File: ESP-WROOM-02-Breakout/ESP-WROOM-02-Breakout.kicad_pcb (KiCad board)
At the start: 2 copper layers, 31.5 x 29 mm, 9 parts, among them IC1 ESP-WROOM-02U__4MB_, J1 Left Pins, J2 Right Pins, J3 UART

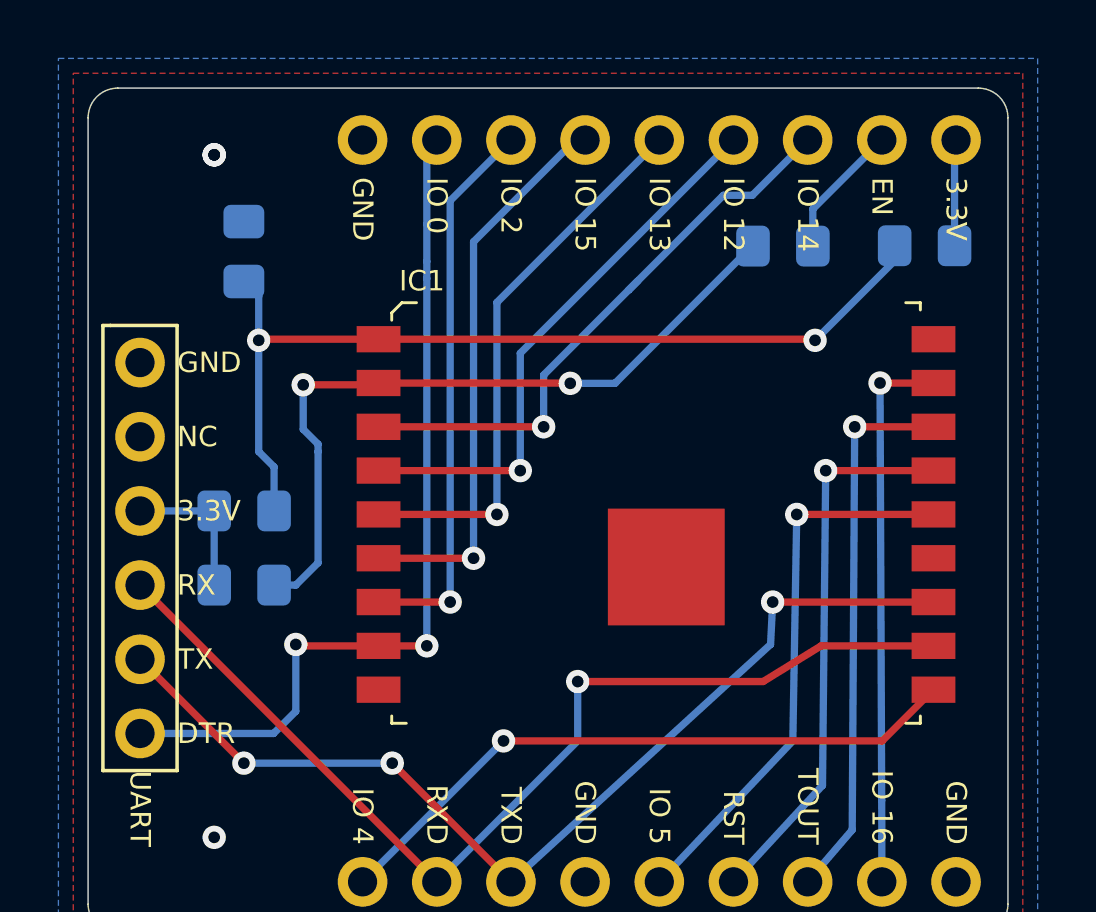
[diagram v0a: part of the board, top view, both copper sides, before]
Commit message: improve esp footprint, small fixes
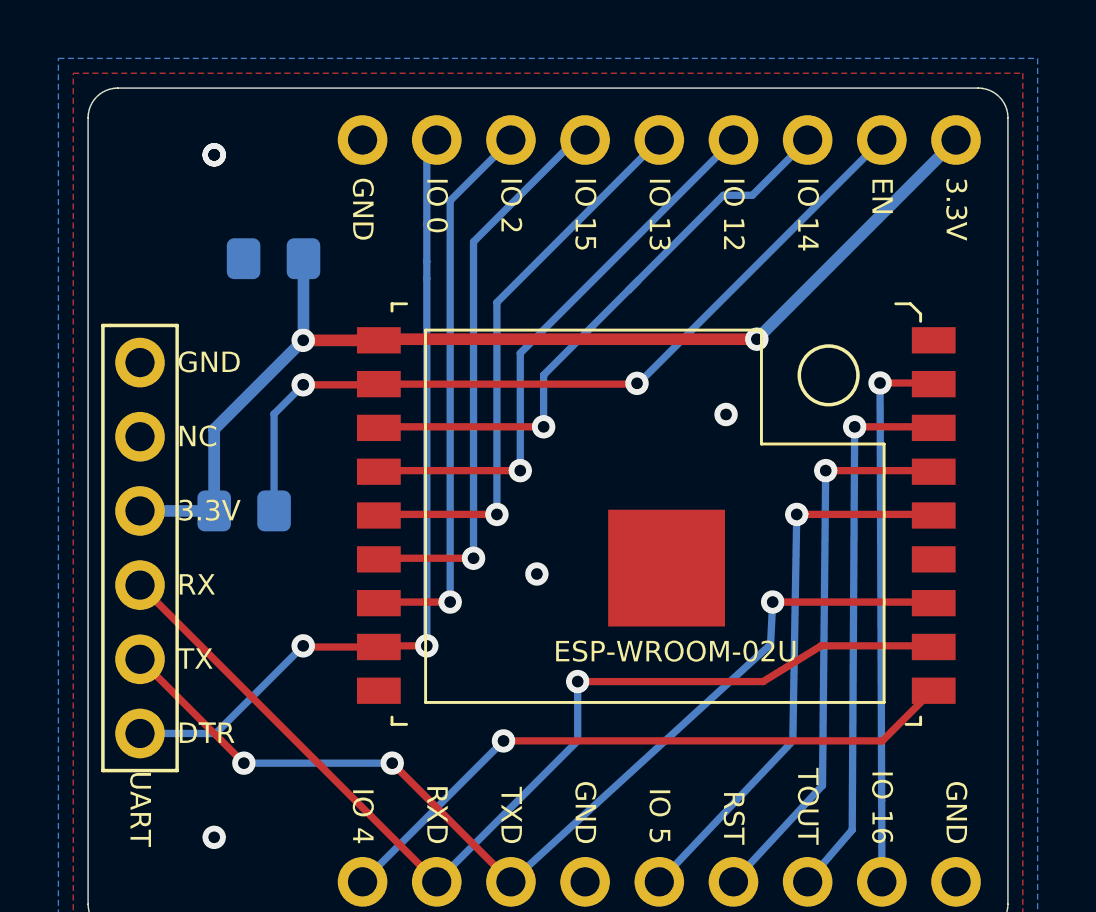
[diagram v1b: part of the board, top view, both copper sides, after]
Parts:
- removed D1, D2, D3: D, Diode_SMD:D_0805_2012Metric_Pad1.15x1.40mm_HandSolder
- moved IC1 8.28 mm to (60.3, 30.6)
- moved R1 2.54 mm to (46.7, 30.5), turned to 0 degrees
- moved C1 1.05 mm to (47.8, 21.8), turned to 180 degrees
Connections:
- C1 pad 1: Net-(C1-Pad1) -> +3V3
- IC1 pad 1: Net-(C1-Pad1) -> +3V3
- IC1 pad 2: Net-(D3-Pad1) -> Net-(IC1-Pad2)
- J1 pad 8: Net-(D3-Pad2) -> Net-(IC1-Pad2)
- J1 pad 9: Net-(D2-Pad2) -> +3V3
- J3 pad 4: Net-(D1-Pad2) -> +3V3
- R1 pad 1: Net-(D3-Pad1) -> +3V3
- R1 pad 2: Net-(D1-Pad2) -> Net-(IC1-Pad2)
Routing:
- net +3V3: track 0.00 -> 37.7 mm, vias 0 -> 2
- net Net-(C1-Pad1): track 31.7 -> 0.00 mm, vias 2 -> 0
- net Net-(IC1-Pad2): track 0.00 -> 28.0 mm, vias 0 -> 2
- net Net-(D3-Pad1): track 25.5 -> 0.00 mm, vias 2 -> 0
- net Net-(D1-Pad2): track 5.08 -> 0.00 mm
- net Net-(D3-Pad2): track 4.64 -> 0.00 mm
- net Net-(D2-Pad2): track 3.67 -> 0.00 mm
- net Net-(IC1-Pad8): track 30.8 -> 29.4 mm
- net GNDREF: vias 3 -> 5

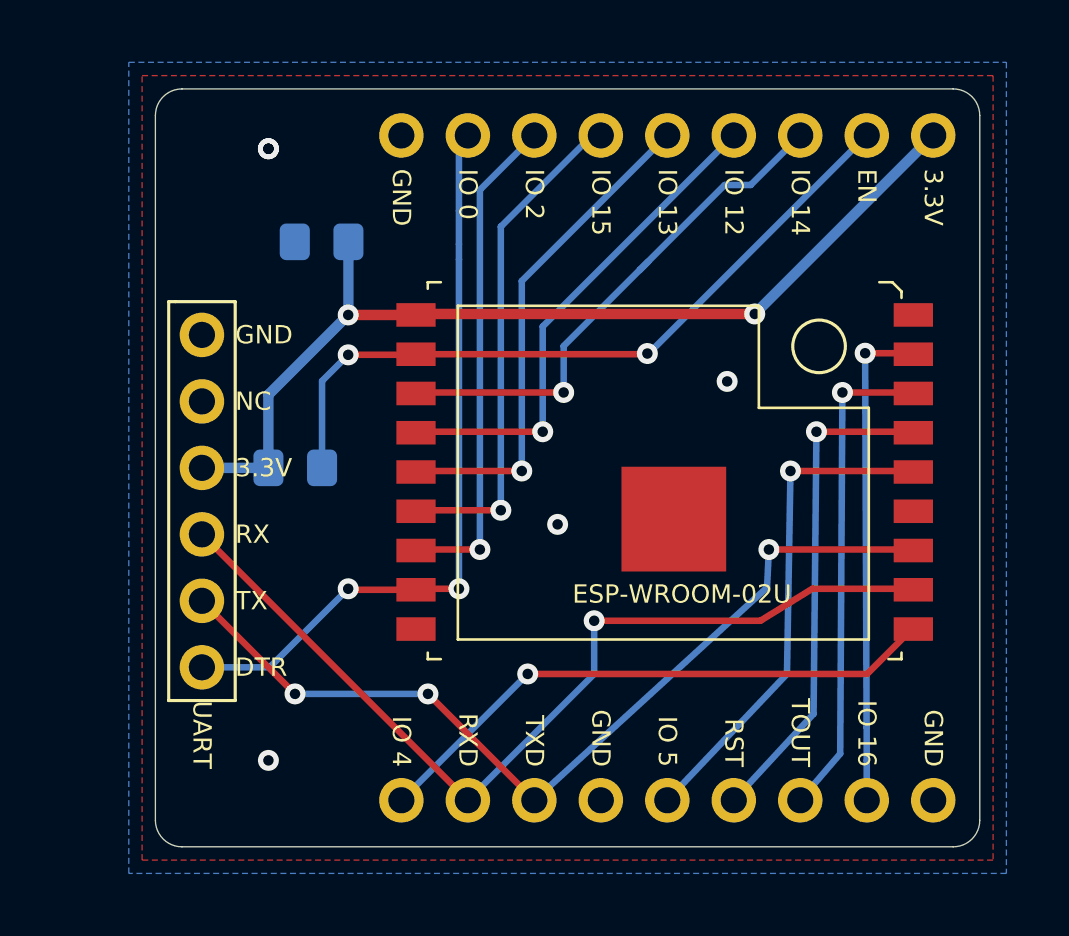
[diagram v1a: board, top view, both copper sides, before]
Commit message: move all components to one side, try to keep it hand-solder friendly
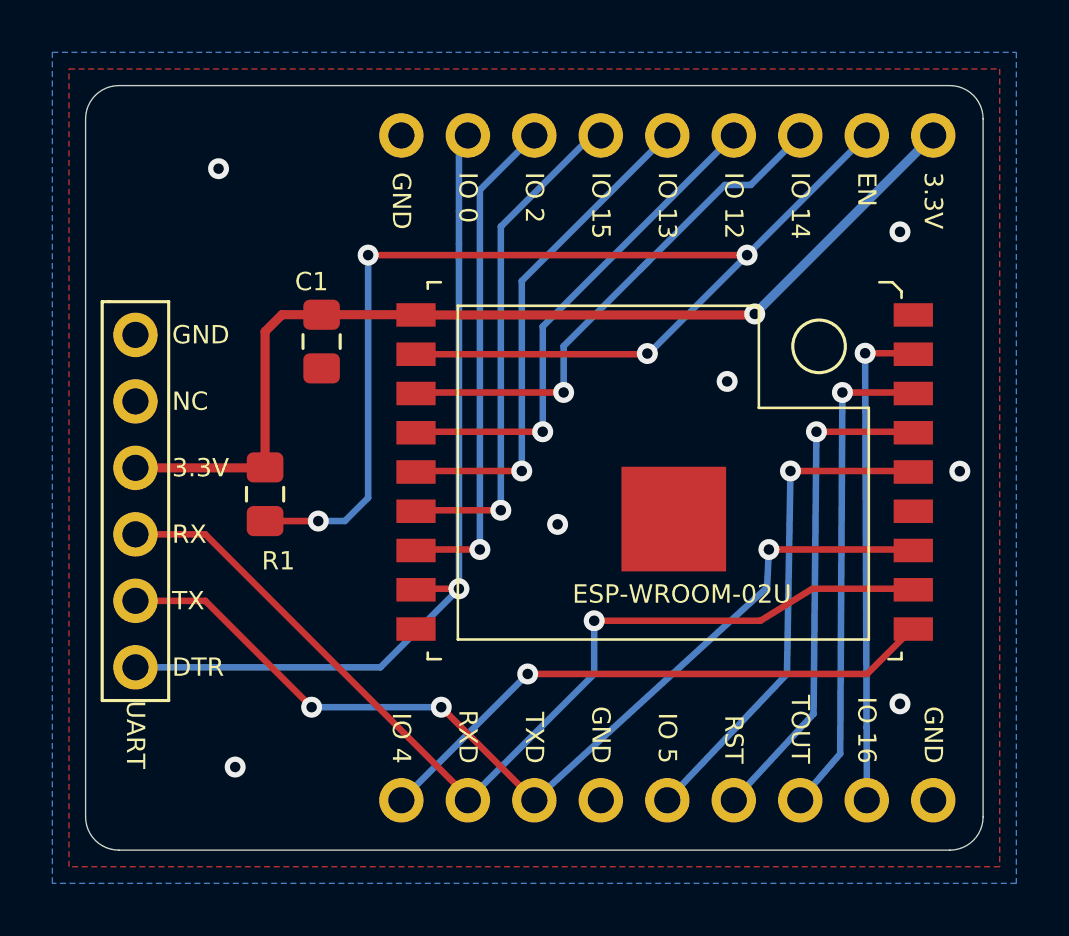
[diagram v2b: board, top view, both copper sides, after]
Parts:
- C1, R1: moved to F.Cu
- moved C1 3.81 mm to (47.8, 25.7), turned to 270 degrees
- moved J3 2.54 mm to (40.6, 31.8)
- moved R1 1.53 mm to (45.6, 31.5), turned to 270 degrees
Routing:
- net Net-(IC1-Pad2): track 28.0 -> 48.8 mm, vias 2 -> 4
- net Net-(IC1-Pad8): track 29.4 -> 33.6 mm, vias 2 -> 1
- net Net-(IC1-Pad11): track 35.8 -> 38.4 mm
- net Net-(IC1-Pad12): track 34.4 -> 36.9 mm
- net +3V3: track 37.7 -> 38.9 mm, vias 2 -> 1
- net GNDREF: vias 5 -> 7
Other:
- board size 31.5 x 29 mm -> 34.3 x 29.2 mm
- net class 3.3V added: clearance 0.25, trace_width 0.35, via_dia 0.8, via_drill 0.4
- board text added: "ESP-WROOM-02U Breakout Board 2020-Jul-12 xrstf.de"
- board text removed: "ESP-WROOM-02U Breakout Board 2020-Jul-09 xrstf.de"

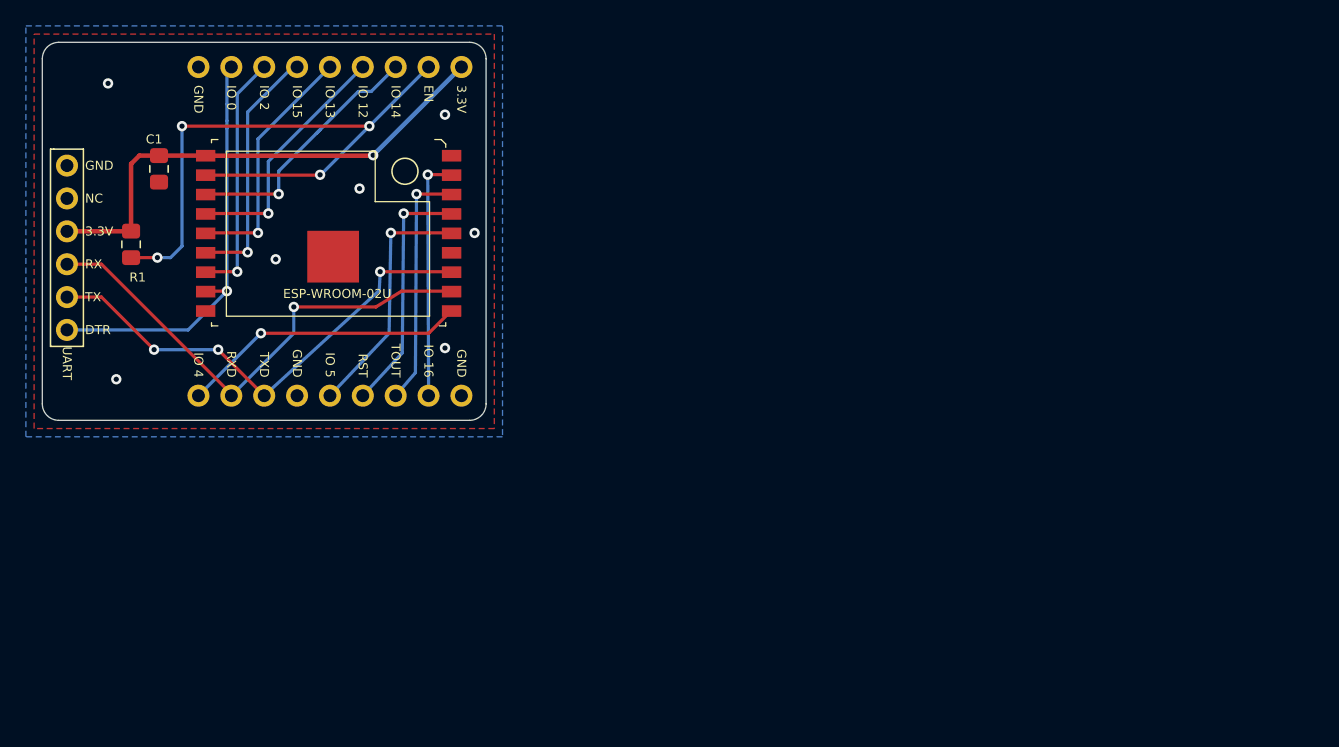
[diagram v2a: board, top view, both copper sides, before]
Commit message: redesign ESP breakout board to be longer and thinner with buttons
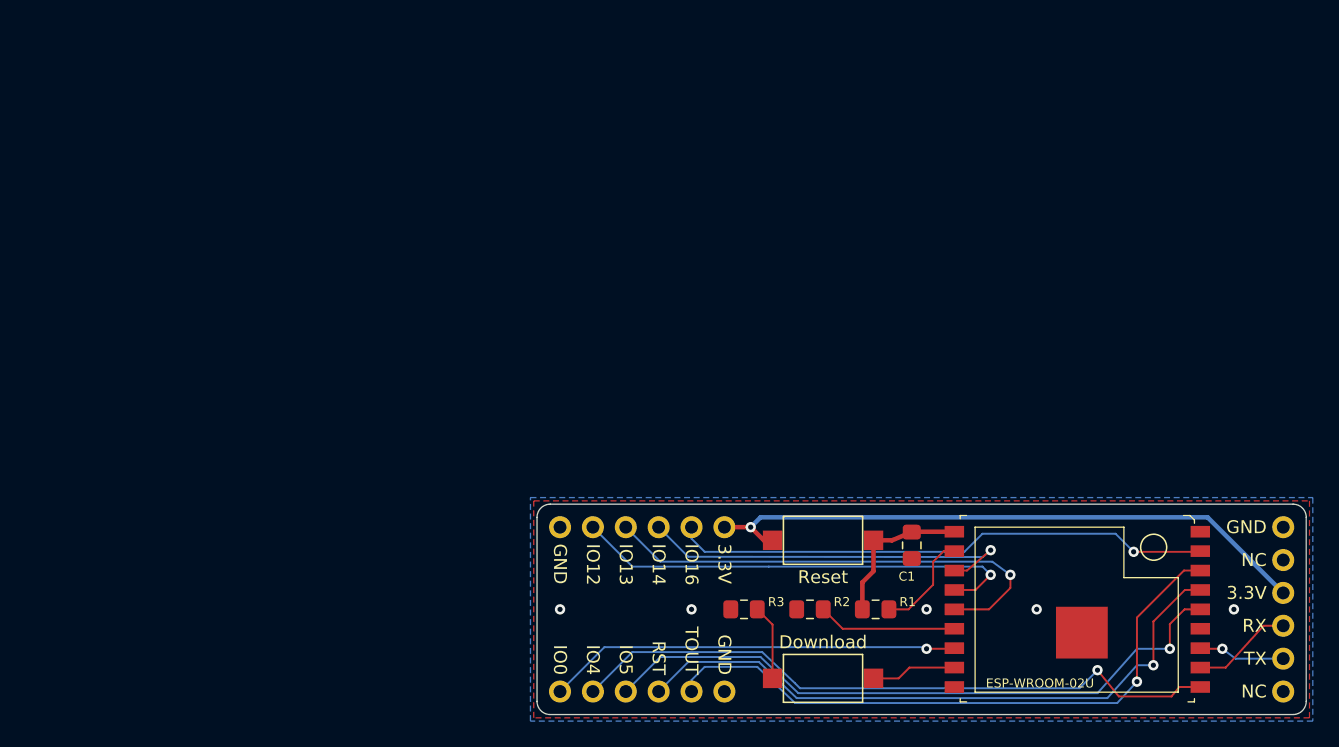
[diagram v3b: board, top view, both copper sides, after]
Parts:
- added Download: DownloadModeBtn, Button_Switch_SMD:SW_SPST_CK_RS282G05A3, F.Cu at (99.1, 65.0)
- added R2: 10K, Resistor_SMD:R_0805_2012Metric_Pad1.15x1.40mm_HandSolder, F.Cu at (98.1, 59.7)
- added R3: 10K, Resistor_SMD:R_0805_2012Metric_Pad1.15x1.40mm_HandSolder, F.Cu at (93.0, 59.7)
- added Reset: ResetBtn, Button_Switch_SMD:SW_SPST_CK_RS282G05A3, F.Cu at (99.1, 54.4)
- J1, J2: footprint ESP-WROOM-02-Breakout:PinHeader_1x09_P2.54mm_Vertical -> ESP-WROOM-02-Breakout:PinHeader_1x06_P2.54mm_Vertical
- moved J3 98.0 mm to (134.6, 59.7)
- moved C1 65.0 mm to (105.9, 54.7)
- moved IC1 64.7 mm to (118.1, 59.7)
- moved R1 64.1 mm to (103.1, 59.7), turned to 0 degrees
- moved J1 49.4 mm to (85.1, 53.3)
- moved J2 26.8 mm to (85.1, 66.0)
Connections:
- C1 pad 1: +3V3 -> /+3.3V
- IC1 pad 1: +3V3 -> /+3.3V
- J1 pad 2: Net-(IC1-Pad8) -> Net-(IC1-Pad4)
- J1 pad 3: Net-(IC1-Pad7) -> Net-(IC1-Pad5)
- J1 pad 4: Net-(IC1-Pad6) -> Net-(IC1-Pad3)
- J1 pad 5: Net-(IC1-Pad5) -> Net-(IC1-Pad17)
- J1 pad 6: Net-(IC1-Pad4) -> +3V3
- J2 pad 2: Net-(IC1-Pad17) -> Net-(IC1-Pad16)
- J2 pad 3: Net-(IC1-Pad16) -> Net-(IC1-Pad15)
- J2 pad 4: Net-(IC1-Pad15) -> Net-(IC1-Pad14)
- J2 pad 5: Net-(IC1-Pad14) -> Net-(IC1-Pad10)
- J2 pad 6: GNDREF -> Net-(IC1-Pad7)
- J3 pad 1: Net-(IC1-Pad8) -> (no net)
- R1 pad 1: +3V3 -> /+3.3V
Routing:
- net Net-(IC1-Pad2): track 48.8 -> 8.53 mm, vias 4 -> 0
- net Net-(IC1-Pad14): track 18.6 -> 50.5 mm
- net Net-(IC1-Pad15): track 18.5 -> 49.4 mm
- net Net-(IC1-Pad11): track 38.4 -> 7.84 mm, vias 1 -> 0
- net Net-(IC1-Pad12): track 36.9 -> 6.68 mm, vias 3 -> 1
- net Net-(IC1-Pad16): track 18.8 -> 48.9 mm
- net Net-(IC1-Pad10): track 22.3 -> 51.2 mm
- net Net-(IC1-Pad8): track 33.6 -> 6.60 mm, vias 1 -> 0
- net Net-(IC1-Pad17): track 18.4 -> 41.8 mm
- net Net-(IC1-Pad5): track 19.7 -> 37.2 mm
- net Net-(IC1-Pad4): track 19.7 -> 35.5 mm
- net Net-(IC1-Pad7): track 19.7 -> 32.0 mm
- net /+3.3V: track 0.00 -> 12.1 mm
- net Net-(IC1-Pad3): track 20.8 -> 30.2 mm
- net +3V3: track 38.9 -> 48.0 mm
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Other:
- board size 34.3 x 29.2 mm -> 59.4 x 16.3 mm
- net class Default: clearance 0.2 -> 0.1; trace_width 0.25 -> 0.15
- rule trace_clearance: 0.2 -> 0.1
- rule trace_min: 0.2 -> 0.1
- rule via_min_drill: 0.3 -> 0.2
- board text added: "ESP-WROOM-02U Breakout Board rev 02 (2020-Jul-18) © xrstf.de (CC BY-SA 4.0)"
- board text added: "IO0"
- board text added: "IO12"
- board text added: "IO13"
- board text added: "IO14"
- board text added: "IO16"
- board text added: "IO4"
- board text added: "IO5"
- board text removed: "DTR"
- board text removed: "EN"
- board text removed: "ESP-WROOM-02U Breakout Board 2020-Jul-12 xrstf.de"
- board text removed: "IO 0"
- board text removed: "IO 12"
- board text removed: "IO 13"
- board text removed: "IO 14"
- board text removed: "IO 15"
- board text removed: "IO 16"
- board text removed: "IO 2"
- board text removed: "IO 4"
- board text removed: "IO 5"
- board text removed: "RXD"
- board text removed: "TXD"
- board text removed: "UART"

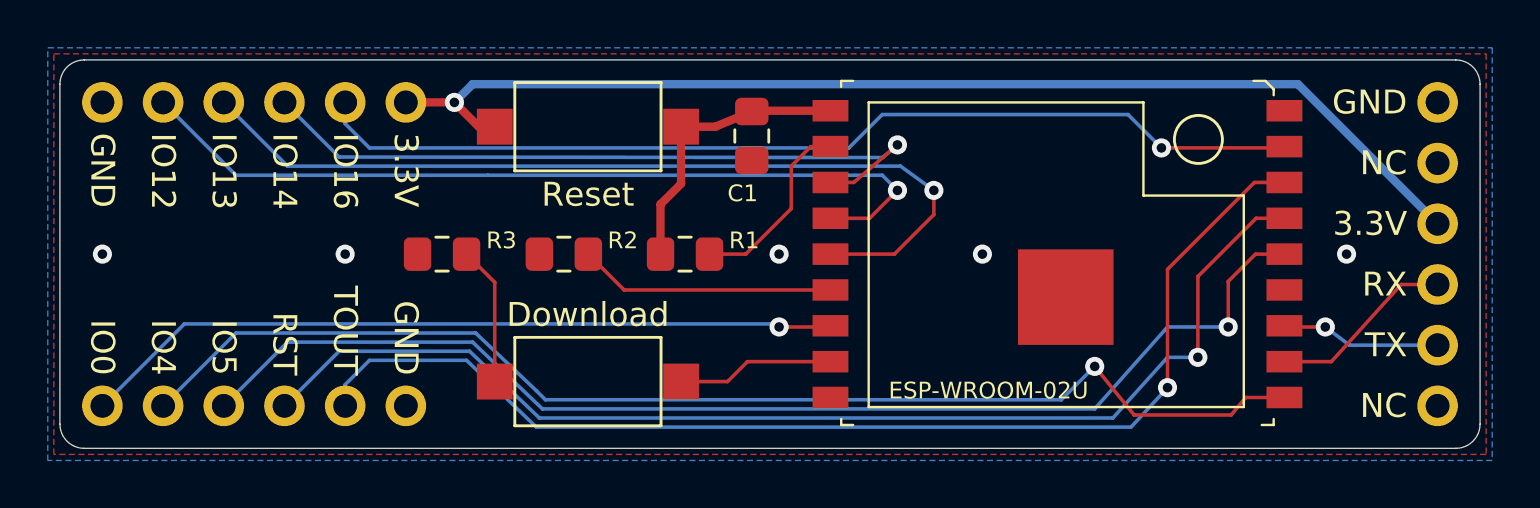
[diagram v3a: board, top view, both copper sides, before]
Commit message: use reset pin instead of cutting power, tidy up a bit
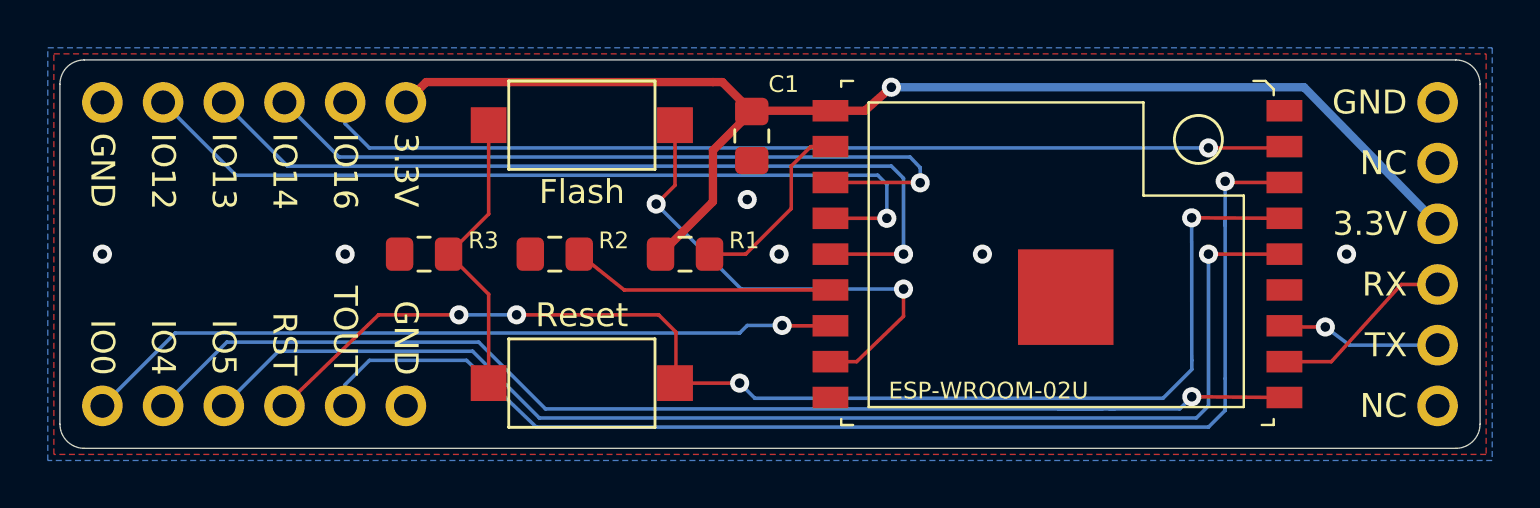
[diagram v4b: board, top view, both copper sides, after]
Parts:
- removed Download: DownloadModeBtn, Button_Switch_SMD:SW_SPST_CK_RS282G05A3
- added Flash: DownloadModeBtn, Button_Switch_SMD:SW_SPST_CK_RS282G05A3, F.Cu at (98.8, 54.3)
- moved Reset 10.7 mm to (98.8, 65.1), turned to 0 degrees
- moved R3 0.75 mm to (92.2, 59.7)
- moved R2 0.38 mm to (97.7, 59.7)
- turned C1 to 90 degrees
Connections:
- C1 pad 1: /+3.3V -> GNDREF
- C1 pad 2: GNDREF -> +3V3
- IC1 pad 1: /+3.3V -> +3V3
- R1 pad 1: /+3.3V -> +3V3
- Reset pad 1: /+3.3V -> Net-(R3-Pad2)
- Reset pad 2: +3V3 -> Net-(IC1-Pad15)
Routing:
- net Net-(IC1-Pad8): track 6.60 -> 20.4 mm, vias 0 -> 2
- net /+3.3V: track 12.1 -> 0.00 mm
- net +3V3: track 48.0 -> 54.7 mm
- net Net-(R3-Pad2): track 5.82 -> 12.2 mm
- net Net-(IC1-Pad15): track 49.4 -> 53.0 mm, vias 1 -> 4
- net Net-(IC1-Pad16): track 48.9 -> 51.8 mm
- net Net-(IC1-Pad14): track 50.5 -> 53.1 mm
- net Net-(IC1-Pad3): track 30.2 -> 32.1 mm
- net Net-(IC1-Pad5): track 37.2 -> 36.0 mm
- net Net-(IC1-Pad17): track 41.8 -> 40.6 mm
- net GNDREF: vias 5 -> 6
